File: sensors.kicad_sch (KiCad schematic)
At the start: 9 parts, among them IC4 BME690, U2 BMP581, U3 BME280

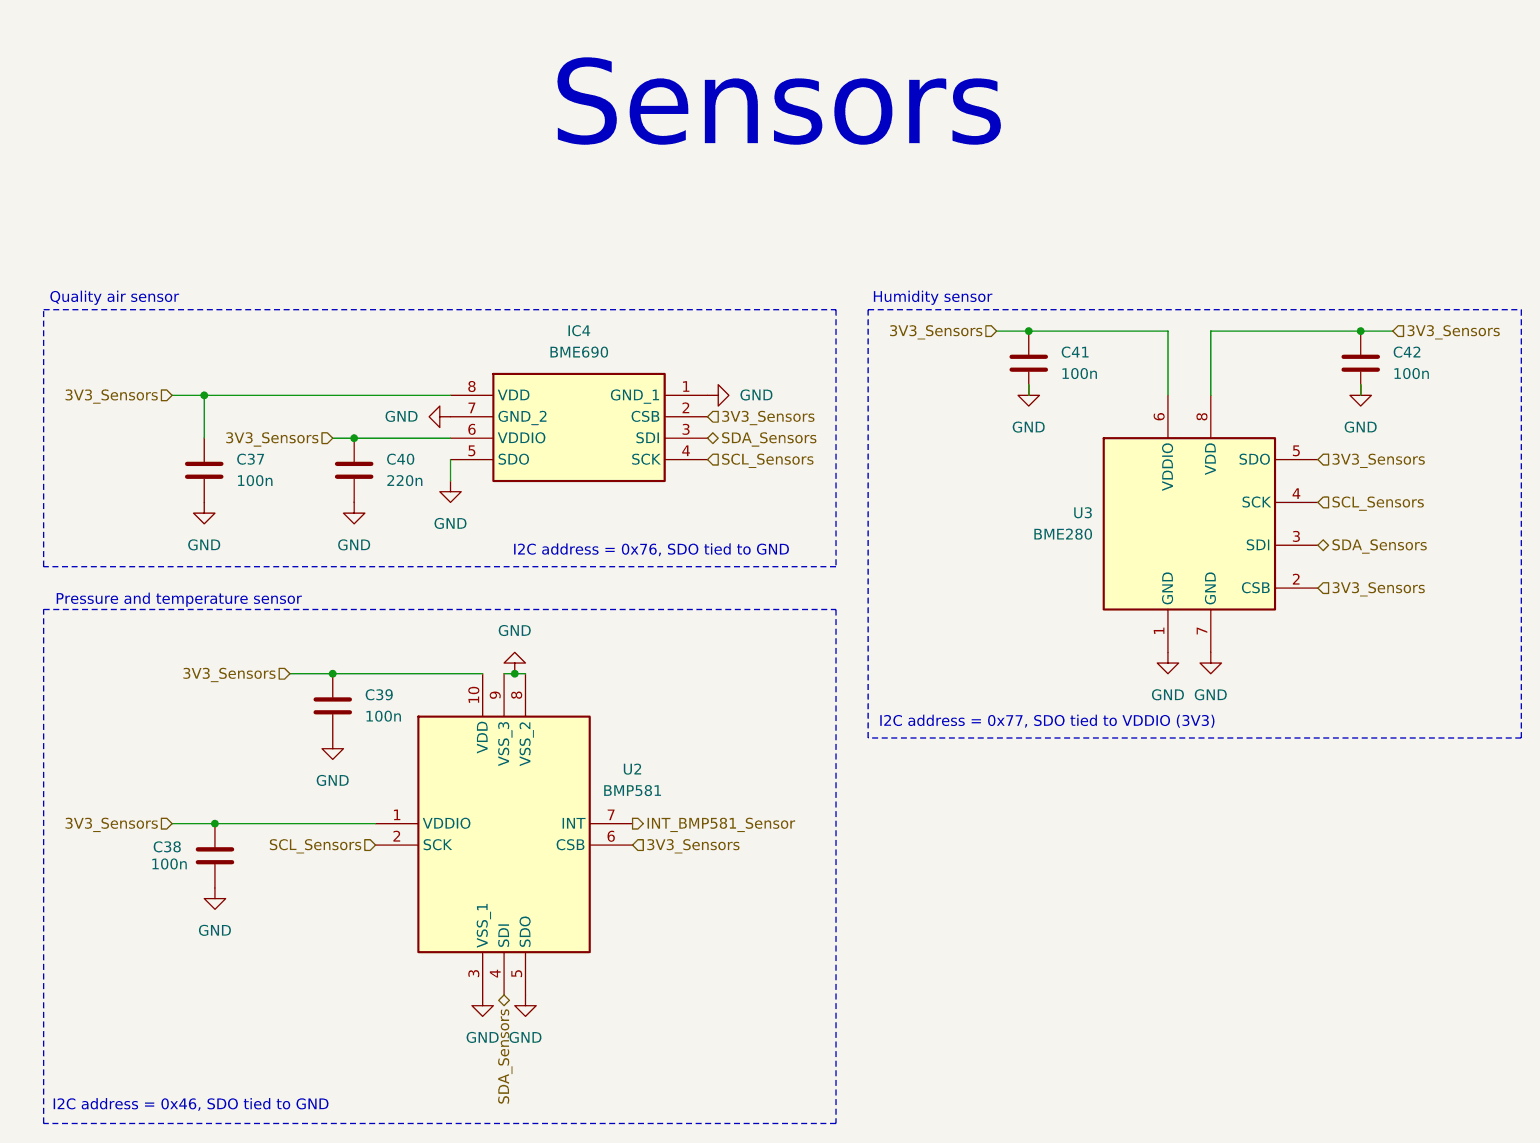
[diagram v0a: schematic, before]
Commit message: Move SWD debug connector from debug sheet to MCU sheet
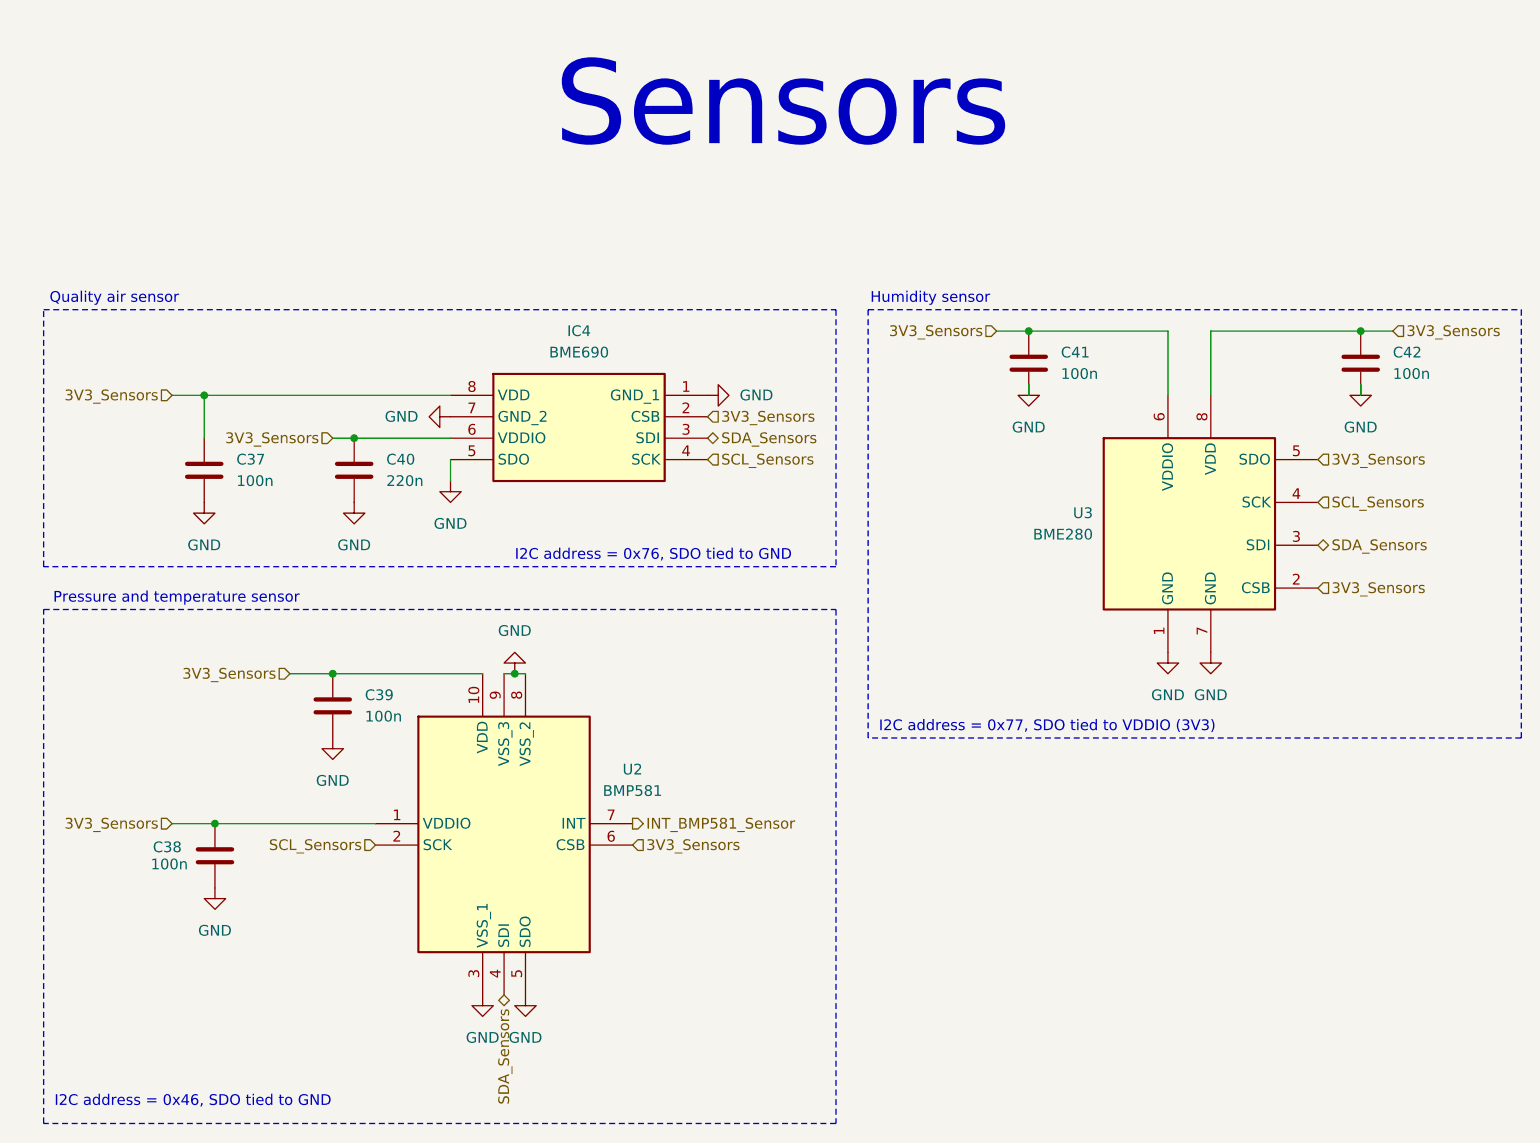
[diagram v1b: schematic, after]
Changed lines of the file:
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@@
 	(text "I2C address = 0x77, SDO tied to VDDIO (3V3)"
 		(exclude_from_sim no)
-		(at 161.29 99.822 0)
+		(at 161.29 100.33 0)
 		(effects
 			(font
@@
 	(text "Humidity sensor"
 		(exclude_from_sim no)
-		(at 167.64 49.53 0)
+		(at 167.386 49.53 0)
 		(effects
 			(font
@@
 	(text "Pressure and temperature sensor"
 		(exclude_from_sim no)
-		(at 78.232 85.344 0)
+		(at 77.978 85.09 0)
 		(effects
 			(font
@@
 	(text "I2C address = 0x46, SDO tied to GND"
 		(exclude_from_sim no)
-		(at 63.246 145.288 0)
+		(at 63.5 144.78 0)
 		(effects
 			(font
@@
 	(text "Sensors"
 		(exclude_from_sim no)
-		(at 149.352 26.67 0)
+		(at 149.86 26.67 0)
 		(effects
 			(font
@@
 	(text "I2C address = 0x76, SDO tied to GND"
 		(exclude_from_sim no)
-		(at 117.856 79.502 0)
+		(at 118.11 80.01 0)
 		(effects
 			(font
